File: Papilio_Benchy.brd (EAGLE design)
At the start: 101.6 x 55.9 mm, 122 parts, among them IC1 FT2232H, SW1 SWITCH-2CH-6P-3010010P1, SW2 EVQQ2, T100 MOSFET-NCHANNELSMD, U1 ARDUINO_MEGA_SHIELD, U100 PCA9306, U101 ATMEGA32U4-XUMU, U2 LTC3419EMS, U3 93C46B, X1 12MHz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

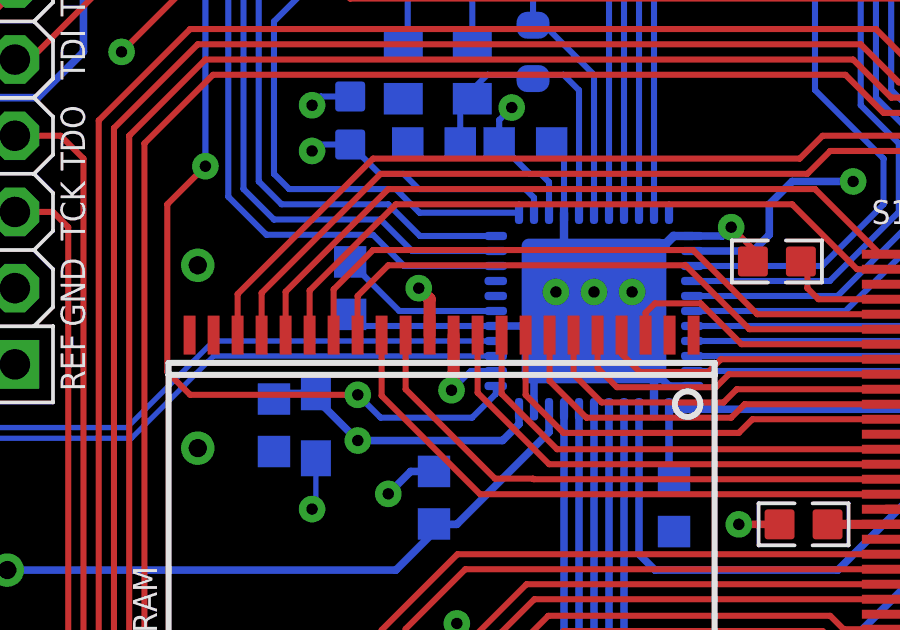
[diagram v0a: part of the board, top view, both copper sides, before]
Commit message: SPI pins moved to same location as the Uno
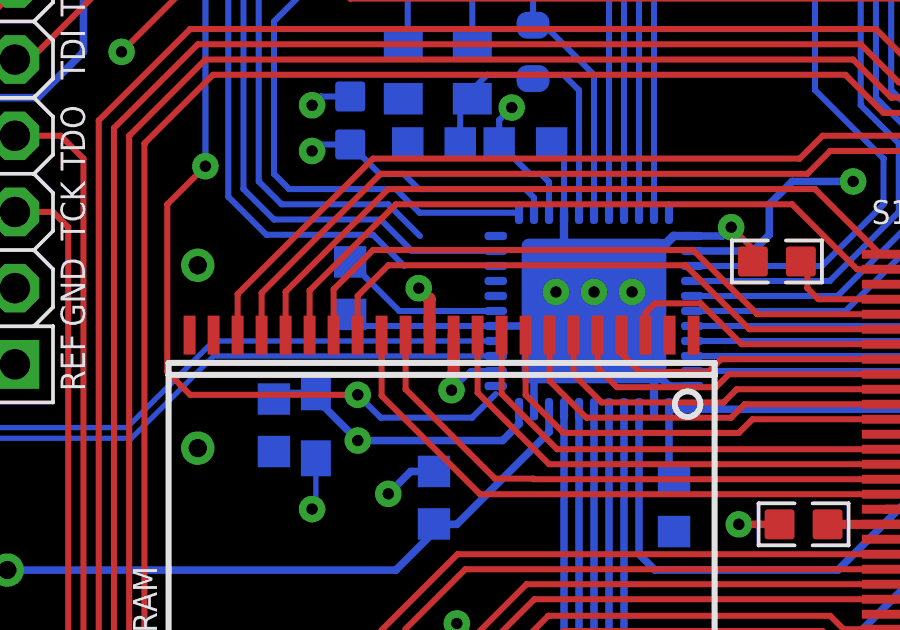
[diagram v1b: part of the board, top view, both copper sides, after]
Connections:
- new net NC: U101.1
- net ATMEGA_IO10*: now also U101.8; no longer U101.11
- net ATMEGA_IO12: now also U101.11; no longer U101.9
- net ATMEGA_IO13*: now also U101.9; no longer U101.1
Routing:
- net ATMEGA_IO12: track 26.6 -> 23.5 mm
- net ATMEGA_IO10*: track 26.5 -> 24.0 mm
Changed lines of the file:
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@@
 <contactref element="R9" pad="2"/>
 <wire x1="31.496" y1="50.8" x2="31.496" y2="53.048" width="0.2032" layer="1"/>
-<contactref element="U101" pad="9"/>
-<wire x1="38.635" y1="34.774" x2="35.584" y2="34.774" width="0.2032" layer="16"/>
 <wire x1="35.584" y1="34.774" x2="34.544" y2="35.814" width="0.2032" layer="16"/>
 <wire x1="34.544" y1="35.814" x2="30.988" y2="35.814" width="0.2032" layer="16"/>
@@
 <wire x1="29.718" y1="37.084" x2="29.718" y2="49.022" width="0.2032" layer="16"/>
 <wire x1="29.718" y1="49.022" x2="31.496" y2="50.8" width="0.2032" layer="16"/>
+<contactref element="U101" pad="11"/>
+<wire x1="35.584" y1="34.774" x2="38.635" y2="35.774" width="0" layer="19" extent="16-16"/>
 </signal>
 <signal name="ATMEGA_D3">
@@
 <contactref element="R11" pad="2"/>
 <wire x1="36.576" y1="50.8" x2="36.576" y2="53.048" width="0.2032" layer="1"/>
-<contactref element="U101" pad="11"/>
-<wire x1="38.635" y1="35.774" x2="36.108" y2="35.774" width="0.2032" layer="16"/>
 <wire x1="36.108" y1="35.774" x2="35.052" y2="36.83" width="0.2032" layer="16"/>
 <wire x1="35.052" y1="36.83" x2="31.496" y2="36.83" width="0.2032" layer="16"/>
@@
 <wire x1="30.734" y1="37.592" x2="30.734" y2="44.958" width="0.2032" layer="16"/>
 <wire x1="30.734" y1="44.958" x2="36.576" y2="50.8" width="0.2032" layer="16"/>
+<contactref element="U101" pad="8"/>
+<wire x1="36.108" y1="35.774" x2="38.635" y2="34.274" width="0" layer="19" extent="16-16"/>
 </signal>
 <signal name="ATMEGA_D5*">
@@
 <wire x1="26.67" y1="48.26" x2="25.235" y2="48.26" width="0.2032" layer="1"/>
 <wire x1="25.235" y1="48.26" x2="23.584" y2="46.609" width="0.2032" layer="1"/>
-<contactref element="U101" pad="1"/>
 <via x="34.036" y="30.48" extent="1-16" drill="0.381"/>
 <wire x1="34.036" y1="30.48" x2="28.448" y2="30.48" width="0.2032" layer="1"/>
@@
 <via x="28.956" y="38.1" extent="1-16" drill="0.381"/>
 <wire x1="28.956" y1="38.1" x2="28.956" y2="50.8" width="0.2032" layer="16"/>
-<wire x1="38.635" y1="30.774" x2="38.635" y2="30.507" width="0.2032" layer="16"/>
 <wire x1="38.635" y1="30.507" x2="37.846" y2="29.718" width="0.2032" layer="16"/>
 <wire x1="37.846" y1="29.718" x2="34.798" y2="29.718" width="0.2032" layer="16"/>
 <wire x1="34.798" y1="29.718" x2="34.036" y2="30.48" width="0.2032" layer="16"/>
+<contactref element="U101" pad="9"/>
+<wire x1="38.635" y1="30.507" x2="38.635" y2="34.774" width="0" layer="19" extent="16-16"/>
 </signal>
 <signal name="ATMEGA_IO8">
@@
 <wire x1="11.633" y1="33.985" x2="12.7" y2="35.052" width="0.6096" layer="1"/>
 </signal>
+<signal name="NC">
+<contactref element="U101" pad="1"/>
+</signal>
 </signals>

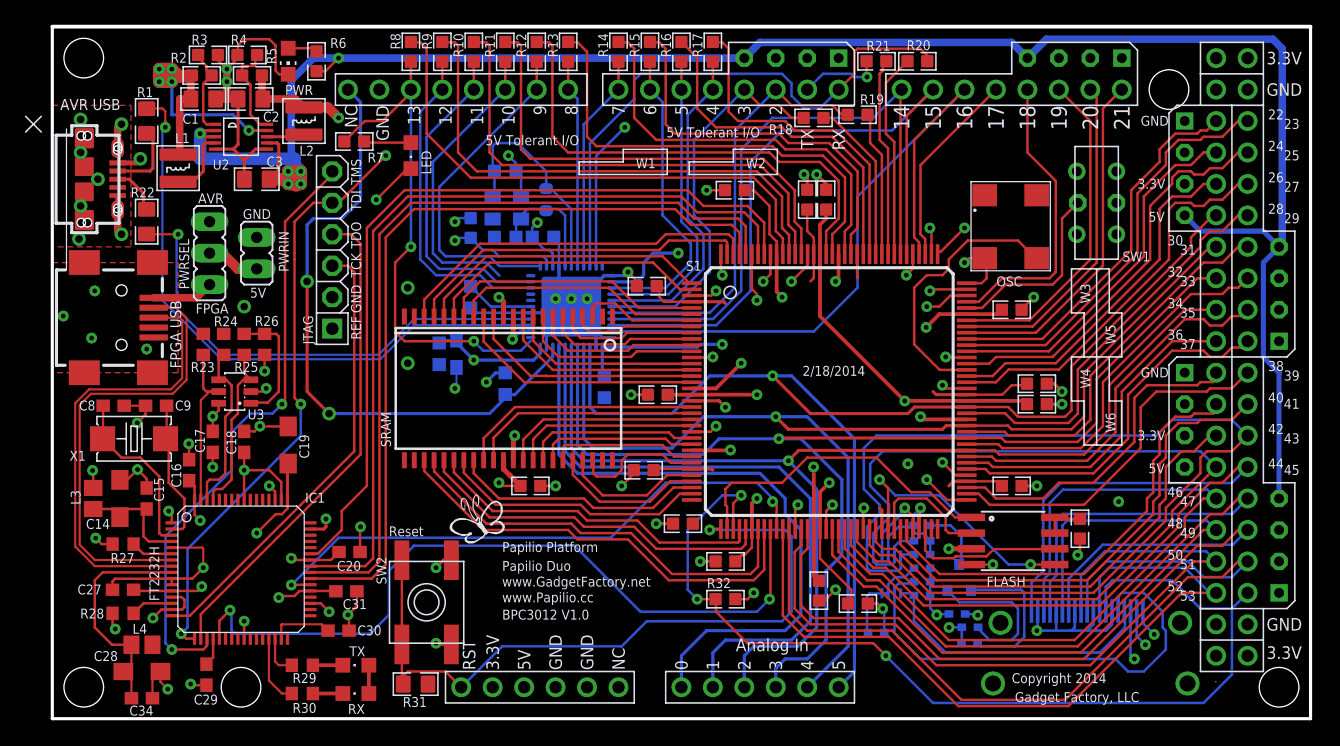
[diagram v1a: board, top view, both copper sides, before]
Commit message: Added more info to silkscreen
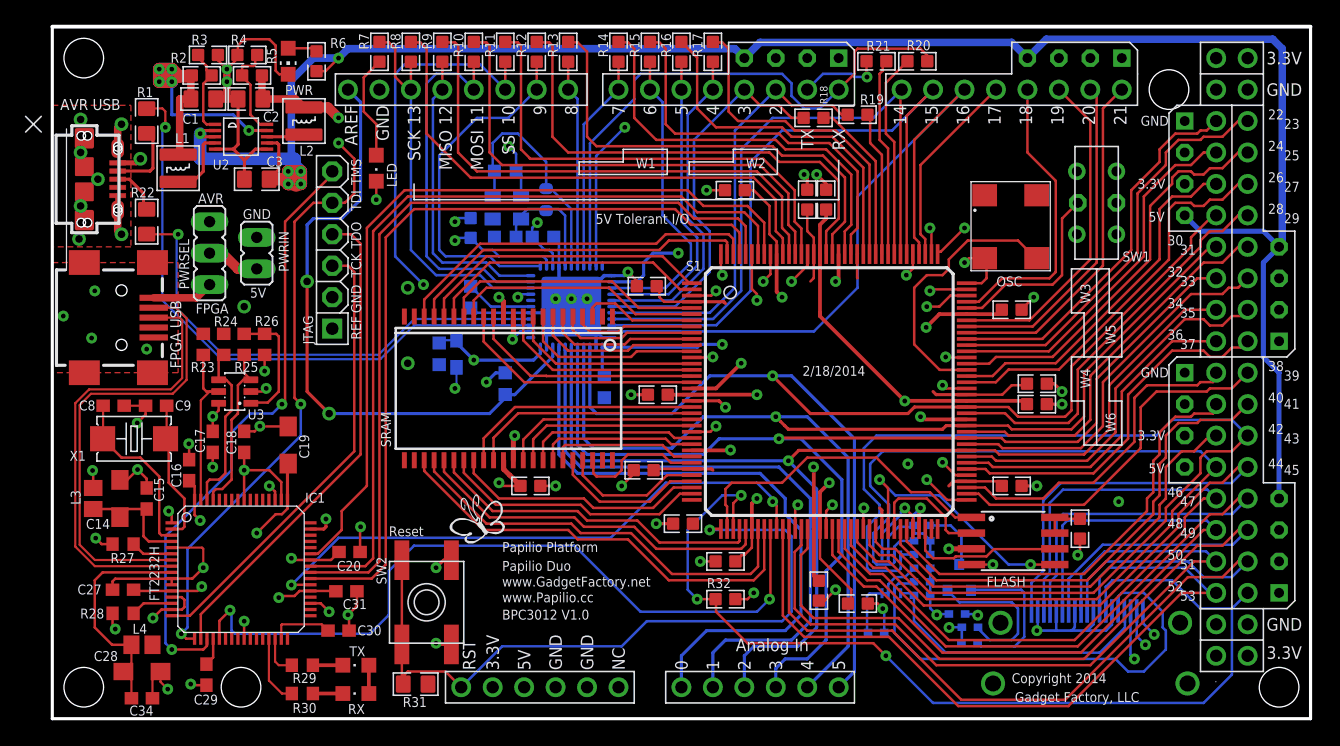
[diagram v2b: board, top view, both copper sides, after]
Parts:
- moved R7 7.52 mm to (26.4, 53.8), turned to 90 degrees
- moved LED 2.97 mm to (26.2, 44.5)
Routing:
- net ATMEGA_IO10*: track 24.0 -> 39.7 mm, vias 0 -> 2
- net ATMEGA_IO13*: track 41.5 -> 31.6 mm, vias 2 -> 0
- net AD1-JTAG_TDI: track 96.8 -> 101.8 mm
- net N$2: track 3.81 -> 8.49 mm
- net ATMEGA_IO11*: track 26.6 -> 30.1 mm
- net GND: track 227.0 -> 225.2 mm
- net ATMEGA_IO9*: track 27.2 -> 28.7 mm
- net XTAL1: track 18.4 -> 19.6 mm
- net ATMEGA_IO12: track 23.5 -> 24.4 mm
- net 5V0: track 296.5 -> 297.1 mm

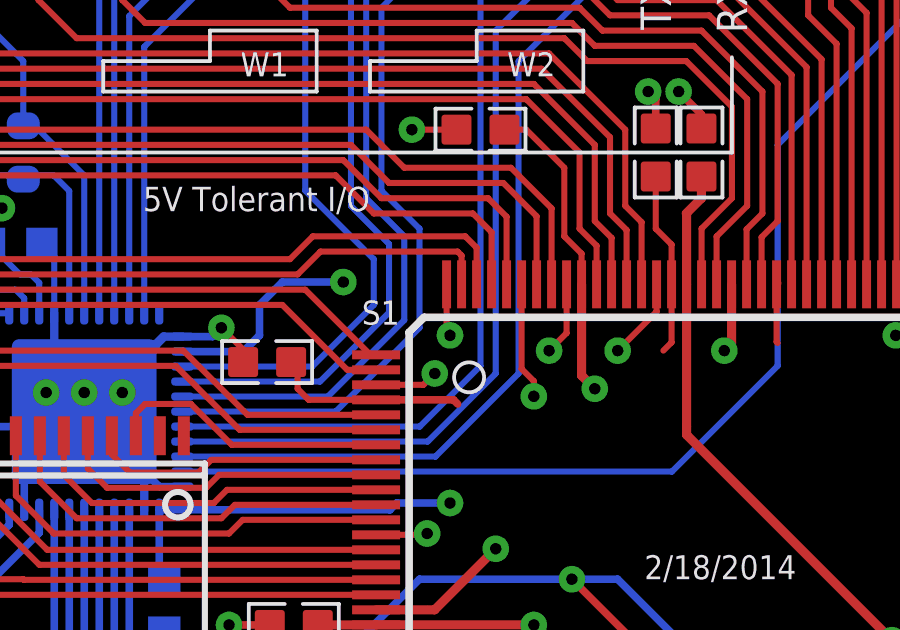
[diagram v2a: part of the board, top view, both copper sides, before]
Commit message: Change HSWAP so I/O floats during config. Cleanup schematic sheets.
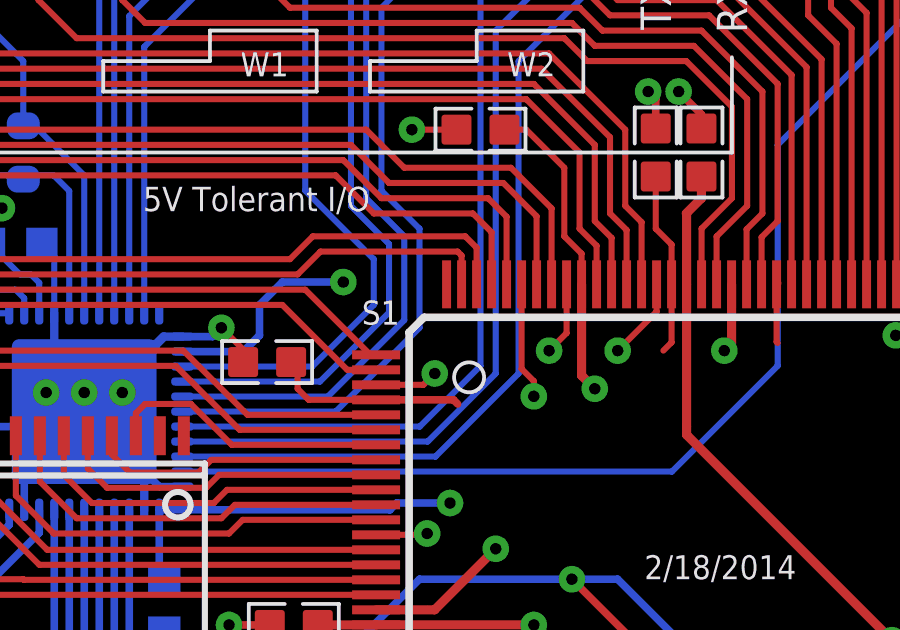
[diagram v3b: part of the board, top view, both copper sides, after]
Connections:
- net 3V3: now also S1.144
- net GND: no longer S1.144
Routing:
- net GND: track 225.2 -> 223.4 mm, vias 76 -> 75
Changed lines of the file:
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@@
 <grid distance="10" unitdist="mil" unit="mil" style="lines" multiple="1" display="no" altdistance="1" altunitdist="mil" altunit="mil"/>
 <layers>
-<layer number="1" name="Top" color="4" fill="1" visible="no" active="yes"/>
+<layer number="1" name="Top" color="4" fill="1" visible="yes" active="yes"/>
 <layer number="2" name="Route2" color="6" fill="1" visible="no" active="yes"/>
 <layer number="3" name="Route3" color="11" fill="1" visible="no" active="yes"/>
 <layer number="14" name="Route14" color="1" fill="6" visible="no" active="no"/>
 <layer number="15" name="Route15" color="5" fill="1" visible="no" active="no"/>
-<layer number="16" name="Bottom" color="1" fill="1" visible="no" active="yes"/>
+<layer number="16" name="Bottom" color="1" fill="1" visible="yes" active="yes"/>
 <layer number="17" name="Pads" color="2" fill="1" visible="yes" active="yes"/>
 <layer number="18" name="Vias" color="2" fill="1" visible="yes" active="yes"/>
@@
 <layer number="22" name="bPlace" color="13" fill="1" visible="yes" active="yes"/>
 <layer number="23" name="tOrigins" color="15" fill="1" visible="yes" active="yes"/>
-<layer number="24" name="bOrigins" color="15" fill="1" visible="no" active="yes"/>
+<layer number="24" name="bOrigins" color="15" fill="1" visible="yes" active="yes"/>
 <layer number="25" name="tNames" color="7" fill="1" visible="yes" active="yes"/>
 <layer number="26" name="bNames" color="7" fill="1" visible="no" active="yes"/>
@@
 <layer number="29" name="tStop" color="12" fill="3" visible="no" active="yes"/>
 <layer number="30" name="bStop" color="12" fill="6" visible="no" active="yes"/>
-<layer number="31" name="tCream" color="7" fill="4" visible="yes" active="yes"/>
+<layer number="31" name="tCream" color="7" fill="4" visible="no" active="yes"/>
 <layer number="32" name="bCream" color="7" fill="5" visible="no" active="yes"/>
 <layer number="33" name="tFinish" color="6" fill="3" visible="no" active="yes"/>
@@
 <layer number="37" name="tTest" color="7" fill="1" visible="no" active="yes"/>
 <layer number="38" name="bTest" color="7" fill="1" visible="no" active="yes"/>
-<layer number="39" name="tKeepout" color="4" fill="11" visible="no" active="yes"/>
-<layer number="40" name="bKeepout" color="1" fill="11" visible="no" active="yes"/>
-<layer number="41" name="tRestrict" color="4" fill="10" visible="no" active="yes"/>
-<layer number="42" name="bRestrict" color="1" fill="10" visible="no" active="yes"/>
-<layer number="43" name="vRestrict" color="2" fill="10" visible="no" active="yes"/>
+<layer number="39" name="tKeepout" color="4" fill="11" visible="yes" active="yes"/>
+<layer number="40" name="bKeepout" color="1" fill="11" visible="yes" active="yes"/>
+<layer number="41" name="tRestrict" color="4" fill="10" visible="yes" active="yes"/>
+<layer number="42" name="bRestrict" color="1" fill="10" visible="yes" active="yes"/>
+<layer number="43" name="vRestrict" color="2" fill="10" visible="yes" active="yes"/>
 <layer number="44" name="Drills" color="7" fill="1" visible="no" active="yes"/>
 <layer number="45" name="Holes" color="7" fill="1" visible="yes" active="yes"/>
@@
 <contactref element="S1" pad="91"/>
 <contactref element="S1" pad="96"/>
-<contactref element="S1" pad="144"/>
 <contactref element="S1" pad="60"/>
 <contactref element="S1" pad="73"/>
@@
 <wire x1="51.638" y1="29.166" x2="53.296" y2="29.166" width="0.2032" layer="1"/>
 <wire x1="53.296" y1="29.166" x2="53.34" y2="29.21" width="0.2032" layer="1"/>
-<wire x1="53.988" y1="35.928" x2="53.988" y2="37.516" width="0.2032" layer="1"/>
-<wire x1="54.102" y1="35.814" x2="53.988" y2="35.928" width="0.2032" layer="1"/>
 <wire x1="57.988" y1="35.89" x2="57.988" y2="37.516" width="0.2032" layer="1"/>
 <wire x1="57.404" y1="35.306" x2="57.988" y2="35.89" width="0.2032" layer="1"/>
@@
 <via x="53.34" y="29.21" extent="1-16" drill="0.381"/>
 <via x="53.594" y="34.544" extent="1-16" drill="0.381"/>
-<via x="54.102" y="35.814" extent="1-16" drill="0.381"/>
 <via x="57.404" y="35.306" extent="1-16" drill="0.381"/>
 <via x="46.736" y="26.162" extent="1-16" drill="0.381"/>
@@
 <via x="55.626" y="28.702" extent="1-16" drill="0.381"/>
 <wire x1="55.626" y1="28.702" x2="55.88" y2="28.702" width="0.3048" layer="3"/>
+<contactref element="S1" pad="144"/>
 </signal>
 <signal name="1V2">

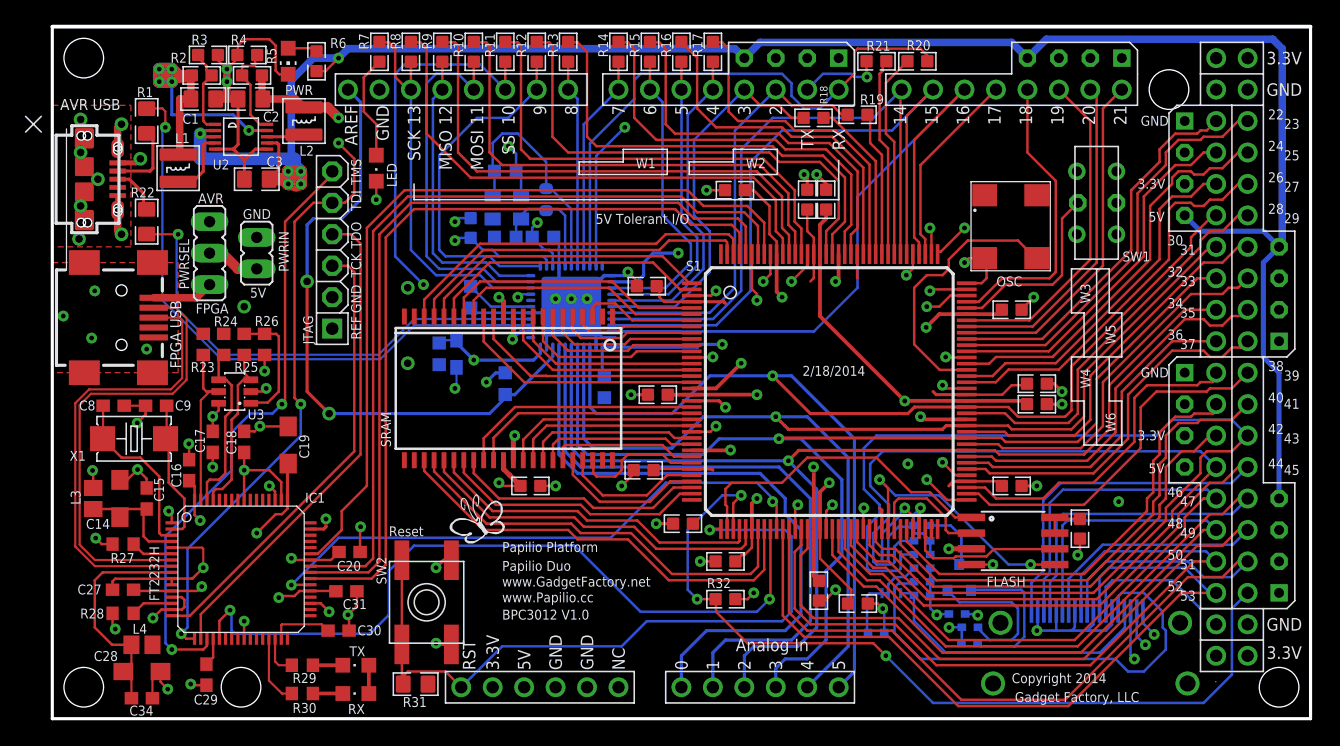
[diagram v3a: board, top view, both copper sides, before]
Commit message: Cleanup silkscreen
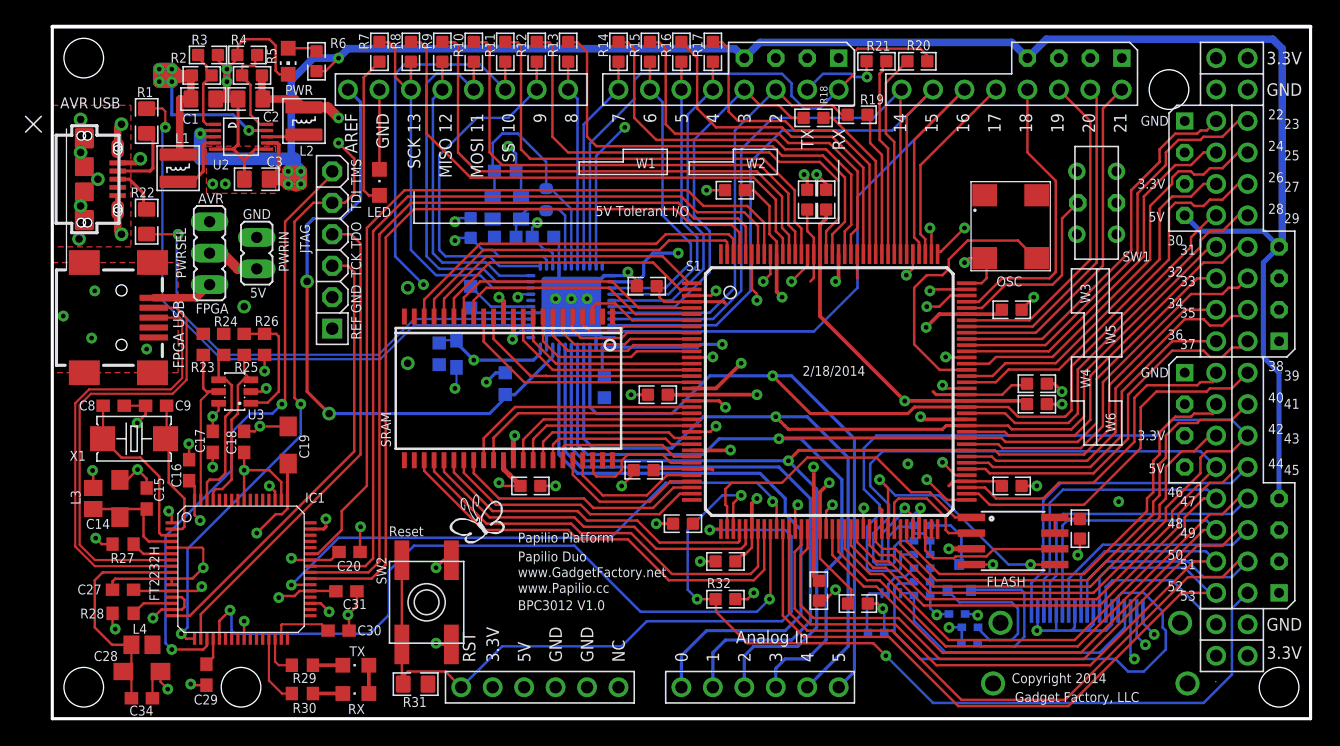
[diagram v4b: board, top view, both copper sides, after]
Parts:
- moved LED 1.17 mm to (26.4, 43.3), turned to 0 degrees
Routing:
- net GND: track 223.4 -> 228.4 mm, vias 75 -> 76
- net N$2: track 8.49 -> 12.3 mm

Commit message: Final fixes as pointed out in the forum.
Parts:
- moved U$7 8.70 mm to (40.5, 14.6)
- moved R31 3.70 mm to (27.9, 6.22), turned to 90 degrees
- moved SW2 3.42 mm to (32.5, 11.9), turned to 0 degrees
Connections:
- net 3V3: now also U1.IOREF; no longer U1.3V3@3, U1.3V3@4
- net 5V0: now also U1.5V@1, U1.5V@2
- net GND: no longer U1.GND@5, U1.GND@6
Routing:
- net 5V0: track 297.1 -> 305.8 mm
- net RESET: track 59.1 -> 66.1 mm
- net GND: track 228.4 -> 229.3 mm
- net 1V2: track 149.6 -> 149.0 mm
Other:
- board text added: "Bottom silkscreen is on layer 200"
- board text added: "Top silkscreen is on layer 130: tSilk"
